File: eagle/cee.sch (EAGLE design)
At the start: 55 parts, among them IC1 IC1, J1 SOLDERJUMPERNC2

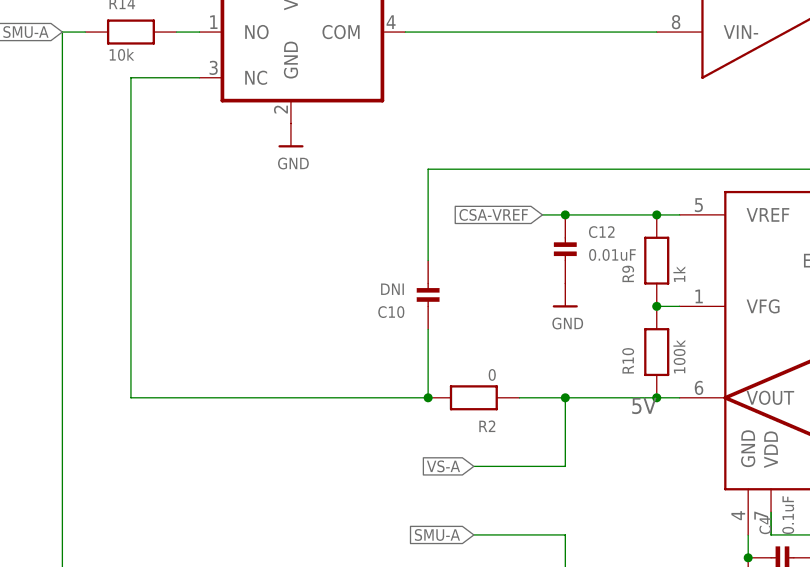
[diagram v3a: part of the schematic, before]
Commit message: Add series resistor with compensation capacitor.
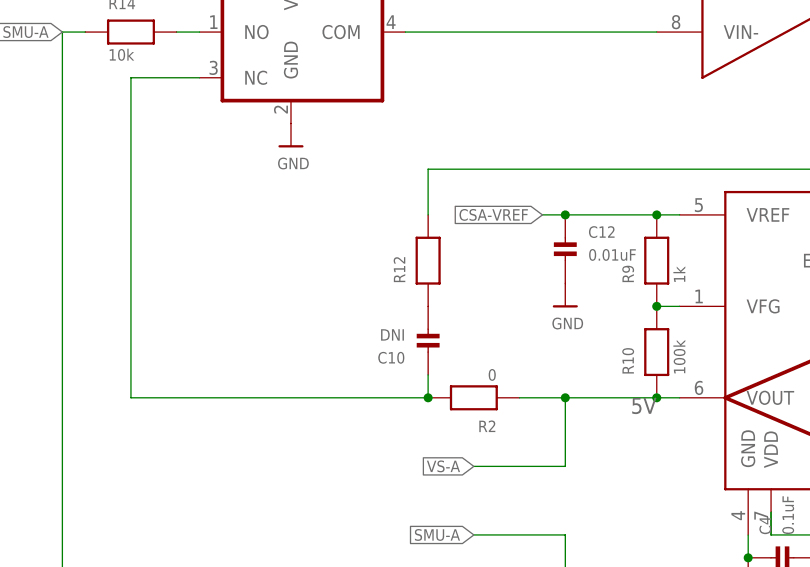
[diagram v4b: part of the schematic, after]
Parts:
- added R12: (no value), nonolith:RESISTOR0603
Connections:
- new net N$14: C10.P$2, R12.1
- net VO-A: now also R12.2; no longer C10.P$2
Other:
- moved on the sheet: C10
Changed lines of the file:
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@@
 <?xml version="1.0" encoding="utf-8"?>
 <!DOCTYPE eagle SYSTEM "eagle.dtd">
-<eagle version="6.3">
+<eagle version="6.1">
 <drawing>
 <settings>
@@
 <part name="U$31" library="nonolith" deviceset="GND" device=""/>
 <part name="U$33" library="nonolith" deviceset="GND" device=""/>
+<part name="R12" library="nonolith" deviceset="RESISTOR" device="0603"/>
 </parts>
 <sheets>
@@
 <instance part="C4" gate="G$1" x="160.02" y="139.7" rot="R90"/>
 <instance part="R2" gate="G$1" x="124.46" y="157.48" rot="R180"/>
-<instance part="C10" gate="G$1" x="119.38" y="170.18" rot="R180"/>
+<instance part="C10" gate="G$1" x="119.38" y="165.1" rot="R180"/>
 <instance part="JP5" gate="A" x="228.6" y="172.72"/>
 <instance part="R5" gate="G$1" x="195.58" y="119.38"/>
@@
 <instance part="U$31" gate="G$1" x="53.34" y="111.76"/>
 <instance part="U$33" gate="G$1" x="119.38" y="96.52"/>
+<instance part="R12" gate="G$1" x="119.38" y="172.72" rot="R90"/>
 </instances>
 <busses>
@@
 <pinref part="RS-A" gate="G$1" pin="1"/>
 <wire x1="187.96" y1="208.28" x2="182.88" y2="208.28" width="0.254" layer="91"/>
-<pinref part="C10" gate="G$1" pin="P$2"/>
-<wire x1="119.38" y1="172.72" x2="119.38" y2="182.88" width="0.254" layer="91"/>
+<wire x1="119.38" y1="177.8" x2="119.38" y2="182.88" width="0.254" layer="91"/>
 <wire x1="119.38" y1="182.88" x2="187.96" y2="182.88" width="0.254" layer="91"/>
 <wire x1="187.96" y1="182.88" x2="187.96" y2="160.02" width="0.254" layer="91"/>
@@
 <junction x="187.96" y="182.88"/>
 <junction x="187.96" y="208.28"/>
+<pinref part="R12" gate="G$1" pin="2"/>
 </segment>
 </net>
@@
 <pinref part="C10" gate="G$1" pin="P$1"/>
 <junction x="119.38" y="157.48"/>
-<wire x1="119.38" y1="165.1" x2="119.38" y2="157.48" width="0.254" layer="91"/>
+<wire x1="119.38" y1="160.02" x2="119.38" y2="157.48" width="0.254" layer="91"/>
 <wire x1="86.36" y1="157.48" x2="119.38" y2="157.48" width="0.254" layer="91"/>
 </segment>
@@
 </segment>
 </net>
+<net name="N$14" class="0">
+<segment>
+<pinref part="R12" gate="G$1" pin="1"/>
+<pinref part="C10" gate="G$1" pin="P$2"/>
+</segment>
+</net>

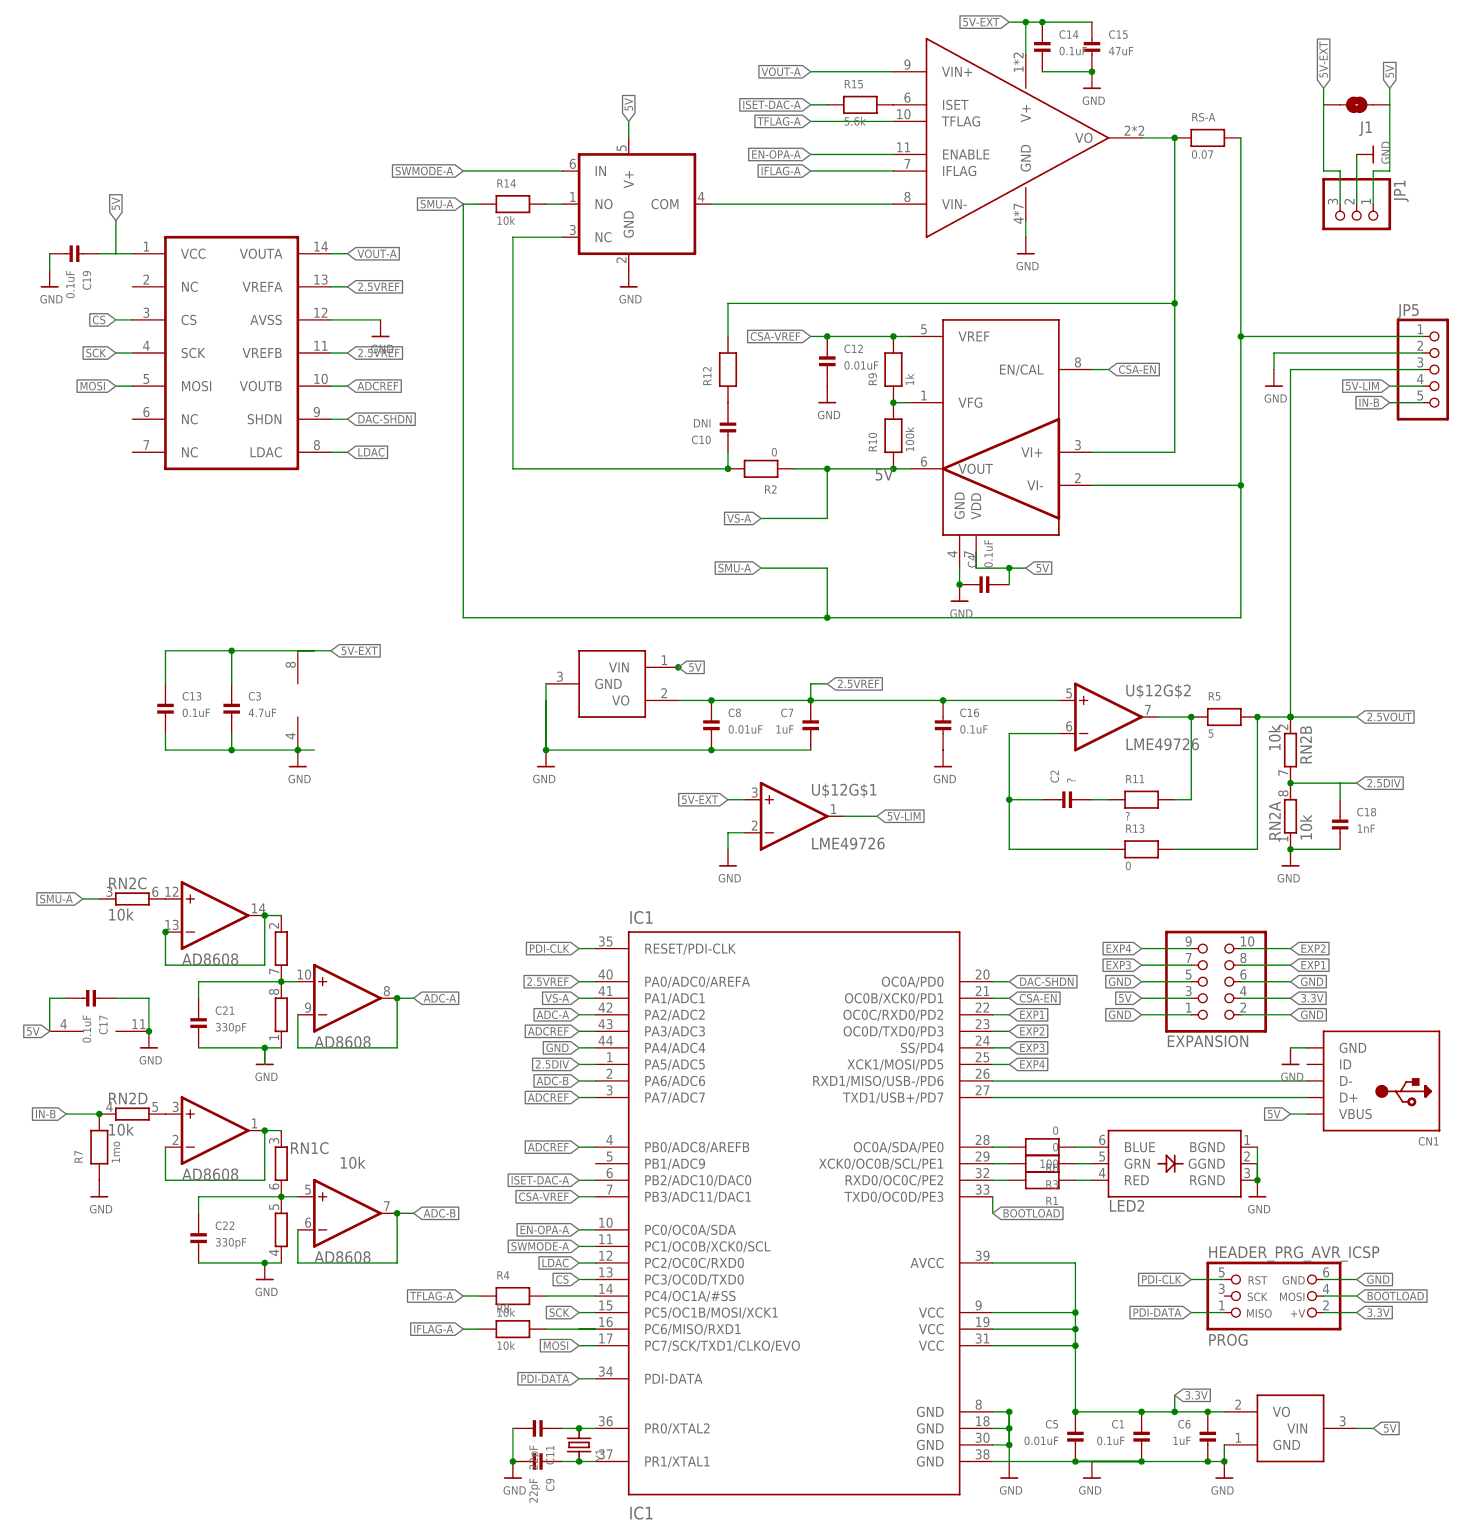
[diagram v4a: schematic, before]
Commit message: renumber parts
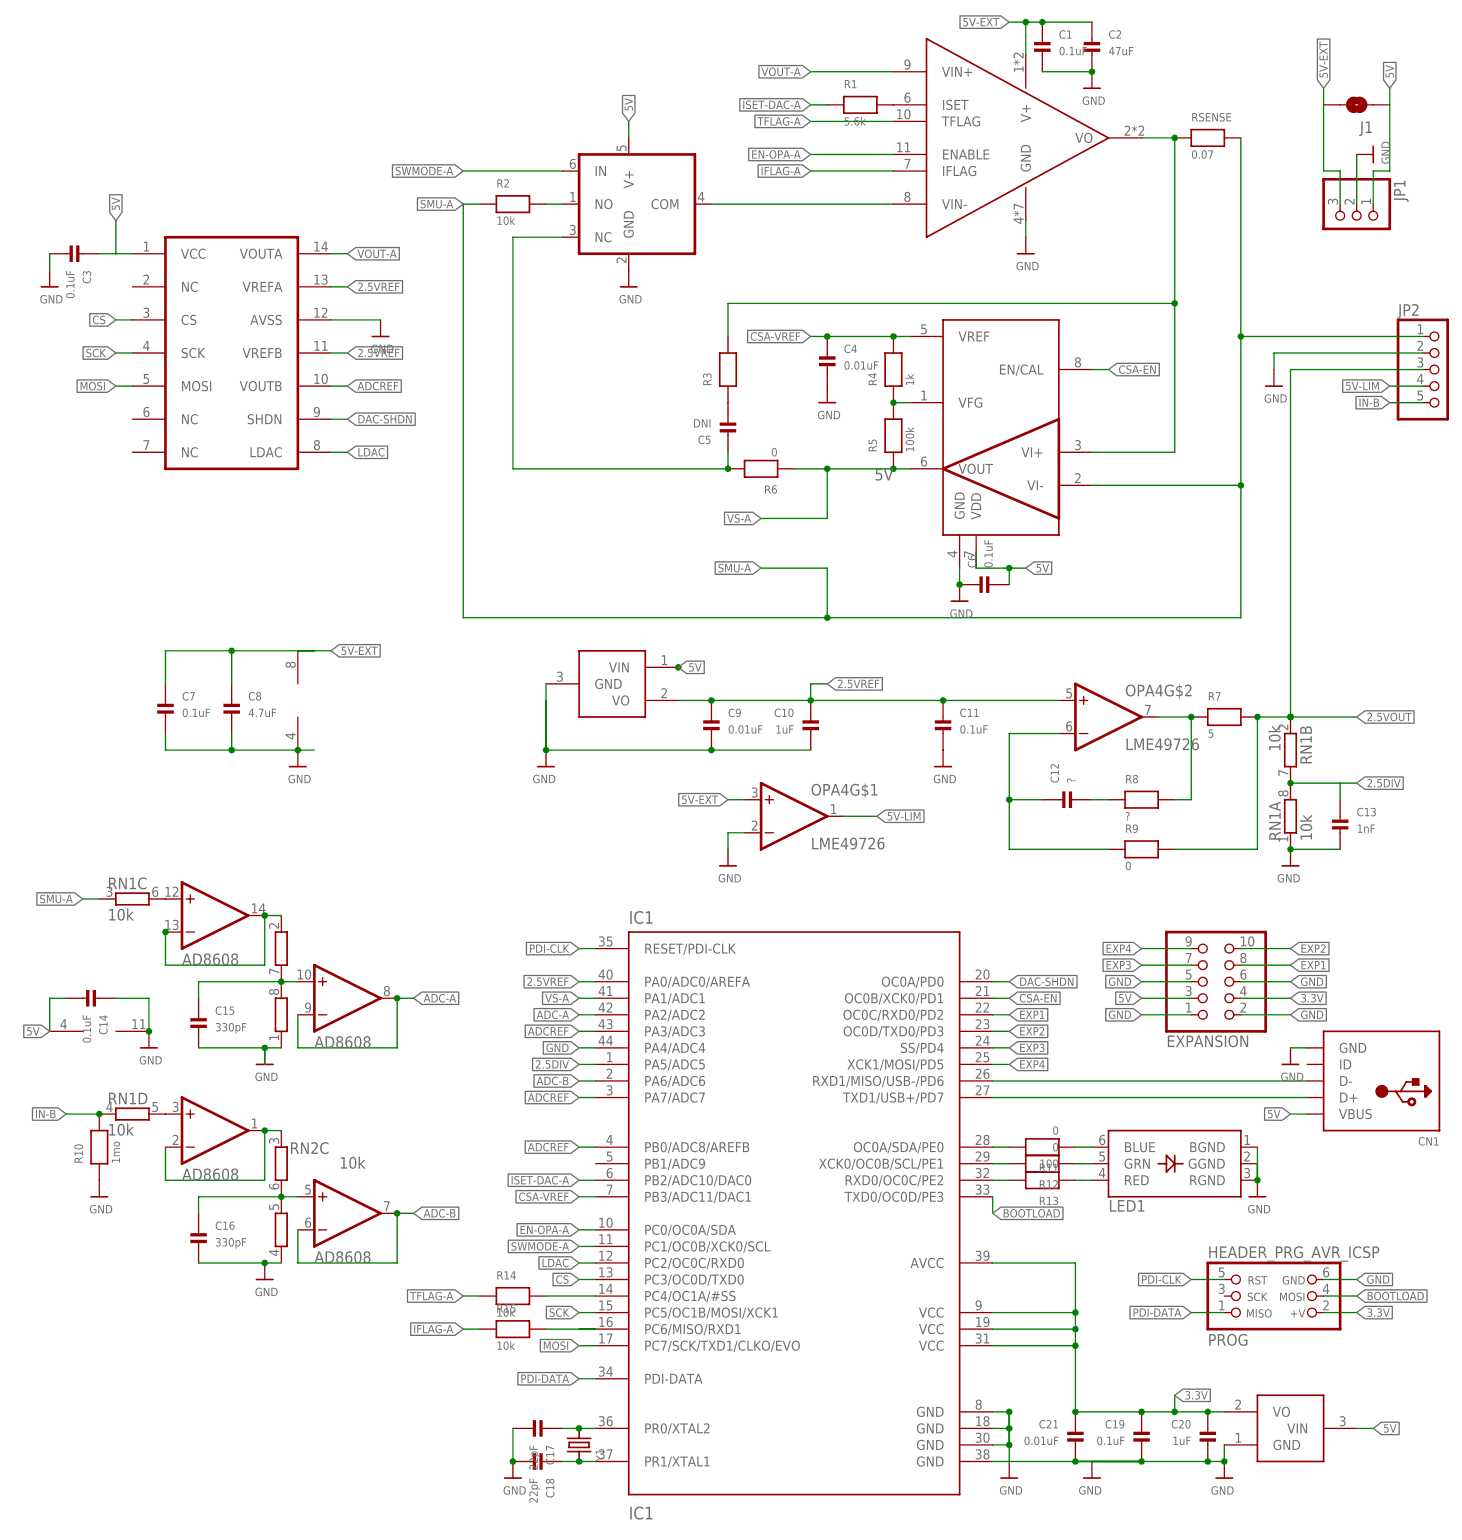
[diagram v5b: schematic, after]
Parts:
- removed C22: 330pF, nonolith:CAP_CERAMIC0603
- added C20: 1uF, nonolith:CAP_CERAMIC0603
- C10: value DNI -> 1uF
- C11: value 22pF -> 0.1uF
- C12: value 0.01uF -> ?
- C13: value 0.1uF -> 1nF
- C15: value 47uF -> 330pF; device nonolith:CAP_CERAMIC1206 -> nonolith:CAP_CERAMIC0603
- C16: value 0.1uF -> 330pF
- C17: value 0.1uF -> 22pF
- C18: value 1nF -> 22pF
- C2: value ? -> 47uF; device nonolith:CAP_CERAMIC0603 -> nonolith:CAP_CERAMIC1206
- C21: value 330pF -> 0.01uF
- C3: value 4.7uF -> 0.1uF
- C4: value 0.1uF -> 0.01uF
- C5: value 0.01uF -> DNI
- C6, C7: value 1uF -> 0.1uF
- C8: value 0.01uF -> 4.7uF
- C9: value 22pF -> 0.01uF
- R1: value 100 -> 5.6k
- R10: value 100k -> 1mo
- R11: value ? -> 0
- R12: value (none) -> 0
- R13: value 0 -> 100
- R15: value 5.6k -> 10k
- R2: value 0 -> 10k
- R3: value 0 -> (none)
- R4: value 10k -> 1k
- R5: value 5 -> 100k; device nonolith:RESISTOR1206 -> nonolith:RESISTOR0603
- R7: value 1mo -> 5; device nonolith:RESISTOR0603 -> nonolith:RESISTOR1206
- R8: value 10k -> ?
- R9: value 1k -> 0
- renumbered DAC to IC2, JP5 to JP2, LED2 to LED1, OPA-A to OPA1, OPA-C to OPA3, RS-A to RSENSE, SW-A to IC3, U$12 to OPA4, U$13 to OPA2
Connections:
- net 2.5DIV: now also C13.P$1, RN1A.2, RN1B.2; no longer C18.P$1, RN2A.2, RN2B.2
- net 2.5VFDBK: now also R7.1, R8.2; no longer R11.2, R5.1
- net 2.5VOUT: now also R7.2, R9.2, RN1B.1; no longer R13.2, R5.2, RN2B.1
- net 2.5VREF: now also C10.P$1, C11.P$1, C9.P$1; no longer C16.P$1, C7.P$1, C8.P$1
- net 3.3V: now also C19.P$1, C20.P$1, C21.P$1; no longer C1.P$1, C5.P$1, C6.P$1
- net 5V: now also C14.P$2, C3.P$1, C6.P$2; no longer C17.P$2, C19.P$1, C4.P$2
- net 5V-EXT: now also C1.P$1, C2.P$1, C7.P$1, C8.P$1; no longer C13.P$1, C14.P$1, C15.P$1, C3.P$1
- net AF-2.5: now also C12.P$2, R8.1; no longer C2.P$2, R11.1
- net AF-A: now also C5.P$1, R6.2; no longer C10.P$1, R2.2
- net BUFF-A: now also RN2B.1; no longer RN1B.1
- net BUFF-B: now also RN2C.1; no longer RN1C.1
- net CSA-VREF: now also C4.P$1, R4.2; no longer C12.P$1, R9.2
- net GND: now also C10.P$2, C14.P$1, C17.P$2, C2.P$2, C20.P$2, C4.P$2, C6.P$1, R10.1, RN2D.1; no longer C12.P$2, C14.P$2, C17.P$1, C22.P$2, C4.P$1, C5.P$2, C6.P$2, R7.1, RN1D.1
- net IFLAG-A: now also R15.1; no longer R8.1
- net IFLAG-P: now also R15.2; no longer R8.2
- net IN-B: now also R10.2, RN1D.1; no longer R7.2, RN2D.1
- net ISET-A: now also R1.2; no longer R15.2
- net ISET-DAC-A: now also R1.1; no longer R15.1
- net N$1: now also C15.P$1, RN2A.2, RN2B.2; no longer C21.P$1, RN1A.2, RN1B.2
- net N$10: now also R13.1; no longer R1.1
- net N$11: now also R12.1; no longer R3.1
- net N$12: now also R11.1; no longer R6.1
- net N$13: now also C12.P$1, R9.1; no longer C2.P$1, R13.1
- net N$14: now also C5.P$2, R3.1; no longer C10.P$2, R12.1
- net N$2: now also C16.P$1, RN2C.2, RN2D.2; no longer C22.P$1, RN1C.2, RN1D.2
- net N$5: now also R13.2; no longer R1.2
- net N$6: now also R12.2; no longer R3.2
- net N$7: now also R11.2; no longer R6.2
- net N$8: now also C18.P$1; no longer C9.P$1
- net N$9: now also C17.P$1; no longer C11.P$1
- net SMU-A: now also R2.1, RN1C.1; no longer R14.1, RN2C.1
- net SMUP-A: now also RN1C.2; no longer RN2C.2
- net SMUP-B: now also RN1D.2; no longer RN2D.2
- net SMUP-SW-A: now also R2.2; no longer R14.2
- net TFLAG-A: now also R14.1; no longer R4.1
- net TFLAG-P: now also R14.2; no longer R4.2
- net VFG: now also R4.1, R5.2; no longer R10.2, R9.1
- net VO-A: now also R3.2; no longer R12.2
- net VS-A: now also R5.1, R6.1; no longer R10.1, R2.1
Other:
- moved on the sheet: C1, C10, C11, C12, C13, C14, C15, C16, C17, C18, C19, C2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

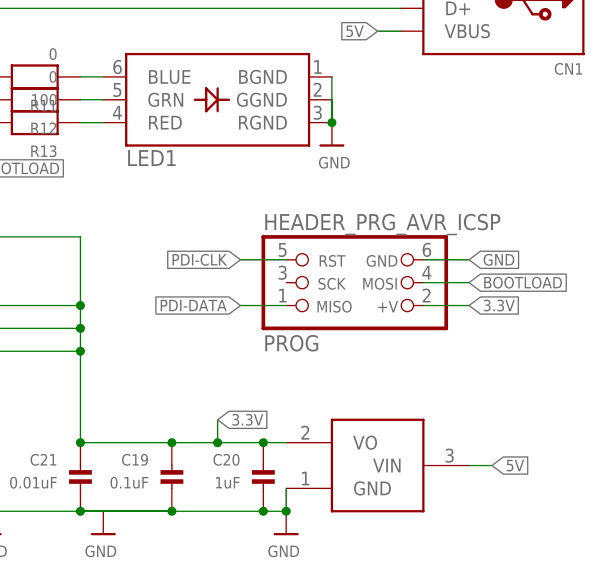
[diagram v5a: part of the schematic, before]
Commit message: Clean up ISP header labels
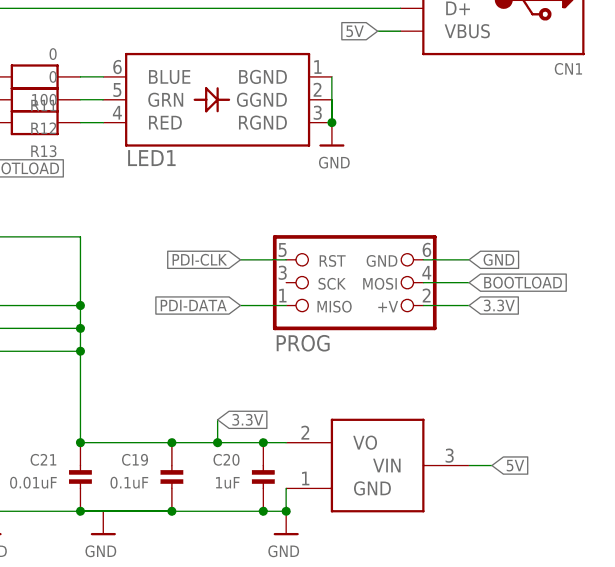
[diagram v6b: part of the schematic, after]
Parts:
- PROG: value HEADER_PRG_AVR_ICSP -> CON_HEADER_PRG_AVR_ICSP; device dp_devices:HEADER_PRG_AVR_ICSP -> nonolith:CON_HEADER_PRG_AVR_ICSP
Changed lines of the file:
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@@
 <part name="C3" library="nonolith" deviceset="CAP_CERAMIC" device="0603" value="0.1uF"/>
 <part name="JP1" library="nonolith" deviceset="HEADER-1X3" device="ROUND"/>
-<part name="PROG" library="dp_devices" deviceset="HEADER_PRG_AVR_ICSP" device=""/>
+<part name="PROG" library="nonolith" deviceset="CON_HEADER_PRG_AVR_ICSP" device=""/>
 <part name="CN1" library="nonolith" deviceset="USB" device="MICROB"/>
 <part name="U$4" library="nonolith" deviceset="GND" device=""/>
@@
 <instance part="C3" gate="G$1" x="17.78" y="190.5" rot="R270"/>
 <instance part="JP1" gate="A" x="215.9" y="195.58" rot="R270"/>
-<instance part="PROG" gate="G$1" x="203.2" y="30.48" rot="MR180"/>
+<instance part="PROG" gate="J" x="203.2" y="30.48" rot="MR180"/>
 <instance part="CN1" gate="G$1" x="218.44" y="63.5" rot="R180"/>
 <instance part="U$4" gate="G$1" x="205.74" y="66.04"/>
@@
 <wire x1="210.82" y1="33.02" x2="215.9" y2="33.02" width="0.254" layer="91"/>
 <label x="215.9" y="33.02" size="1.27" layer="95" rot="MR180" xref="yes"/>
-<pinref part="PROG" gate="G$1" pin="GND"/>
+<pinref part="PROG" gate="J" pin="GND"/>
 </segment>
 <segment>
@@
 <wire x1="195.58" y1="27.94" x2="190.5" y2="27.94" width="0.254" layer="91"/>
 <label x="190.5" y="27.94" size="1.27" layer="95" rot="MR0" xref="yes"/>
-<pinref part="PROG" gate="G$1" pin="MISO"/>
+<pinref part="PROG" gate="J" pin="MISO"/>
 </segment>
 </net>
@@
 <wire x1="195.58" y1="33.02" x2="190.5" y2="33.02" width="0.254" layer="91"/>
 <label x="190.5" y="33.02" size="1.27" layer="95" rot="MR0" xref="yes"/>
-<pinref part="PROG" gate="G$1" pin="RST"/>
+<pinref part="PROG" gate="J" pin="RST"/>
 </segment>
 </net>
@@
 <wire x1="215.9" y1="27.94" x2="210.82" y2="27.94" width="0.254" layer="91"/>
 <label x="215.9" y="27.94" size="1.27" layer="95" rot="MR180" xref="yes"/>
-<pinref part="PROG" gate="G$1" pin="+V"/>
+<pinref part="PROG" gate="J" pin="+V"/>
 </segment>
 </net>
@@
 <wire x1="215.9" y1="30.48" x2="210.82" y2="30.48" width="0.254" layer="91"/>
 <label x="215.9" y="30.48" size="1.27" layer="95" rot="MR180" xref="yes"/>
-<pinref part="PROG" gate="G$1" pin="MOSI"/>
-</segment>
-<segment>
+<pinref part="PROG" gate="J" pin="MOSI"/>
+</segment>
+<segment>
